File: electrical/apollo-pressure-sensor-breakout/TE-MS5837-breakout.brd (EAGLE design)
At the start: 25 x 36 mm, 12 parts, among them U1 TE-MS5837, X1 RJ45-8-2-CONEC-1, X2 M04X2

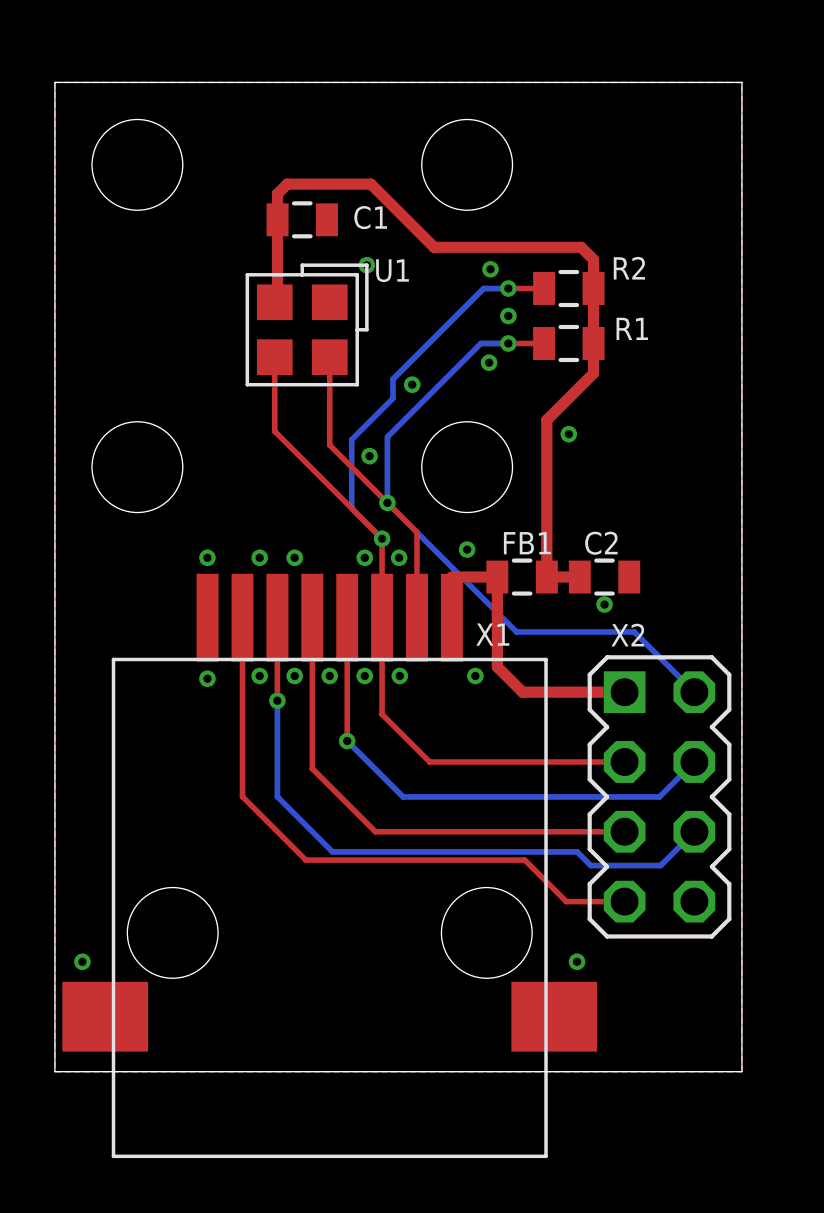
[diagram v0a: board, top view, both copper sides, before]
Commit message: add gerbers to separate directory
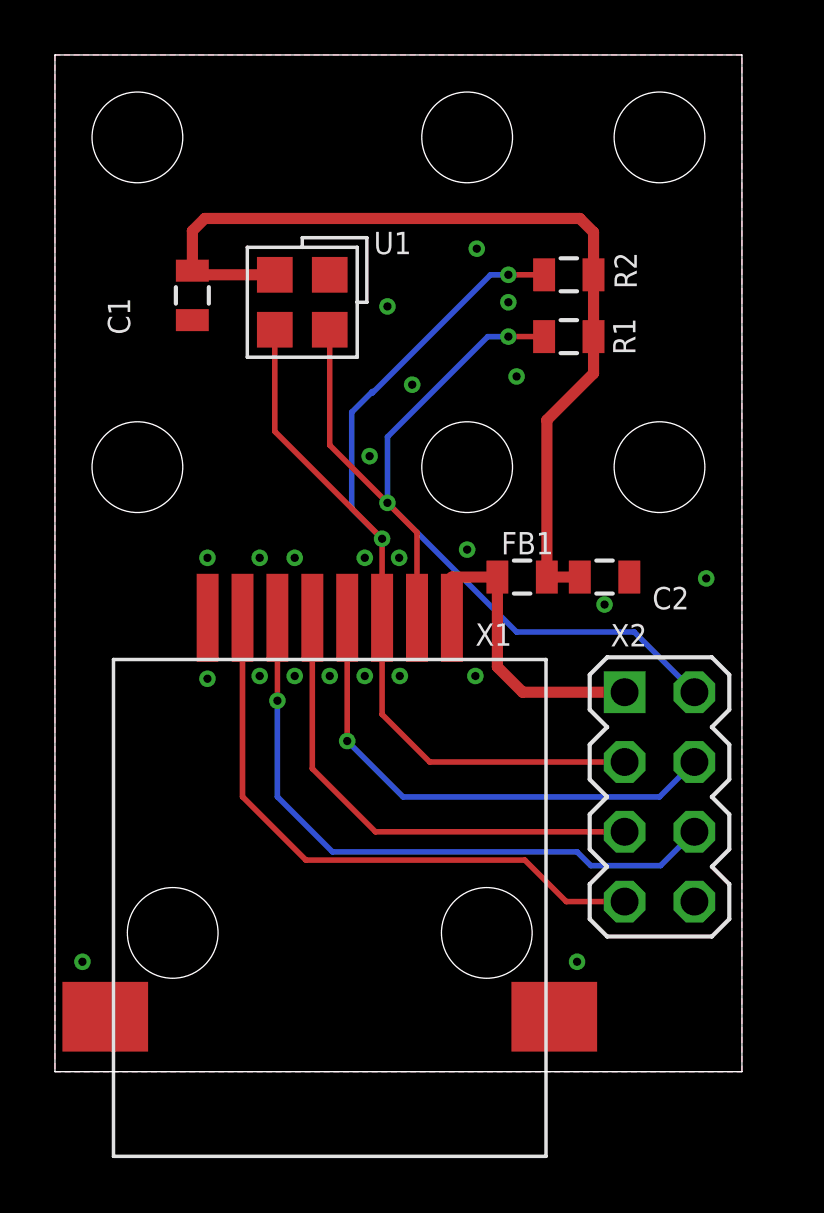
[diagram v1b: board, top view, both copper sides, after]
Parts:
- added JP5, JP6: STAND-OFF, apollo-ctrl:STAND-OFF
- moved C1 4.85 mm to (5.00, 28.2), turned to 270 degrees
- moved JP1 1.00 mm to (3.00, 34.0)
- moved JP2 1.00 mm to (15.0, 34.0)
- moved U1 1.00 mm to (9.00, 28.0)
- moved R2 0.50 mm to (18.7, 29.0)
- moved R1 0.25 mm to (18.7, 26.8)
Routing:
- net 3.3V: track 30.3 -> 34.1 mm
- net SCL: track 37.9 -> 39.4 mm
- net SDA: track 34.3 -> 35.4 mm
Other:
- board size 25 x 36 mm -> 25 x 37 mm
- board text added: "TE MS5837 board Rev. C"

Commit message: resize TE board, add mounting holes
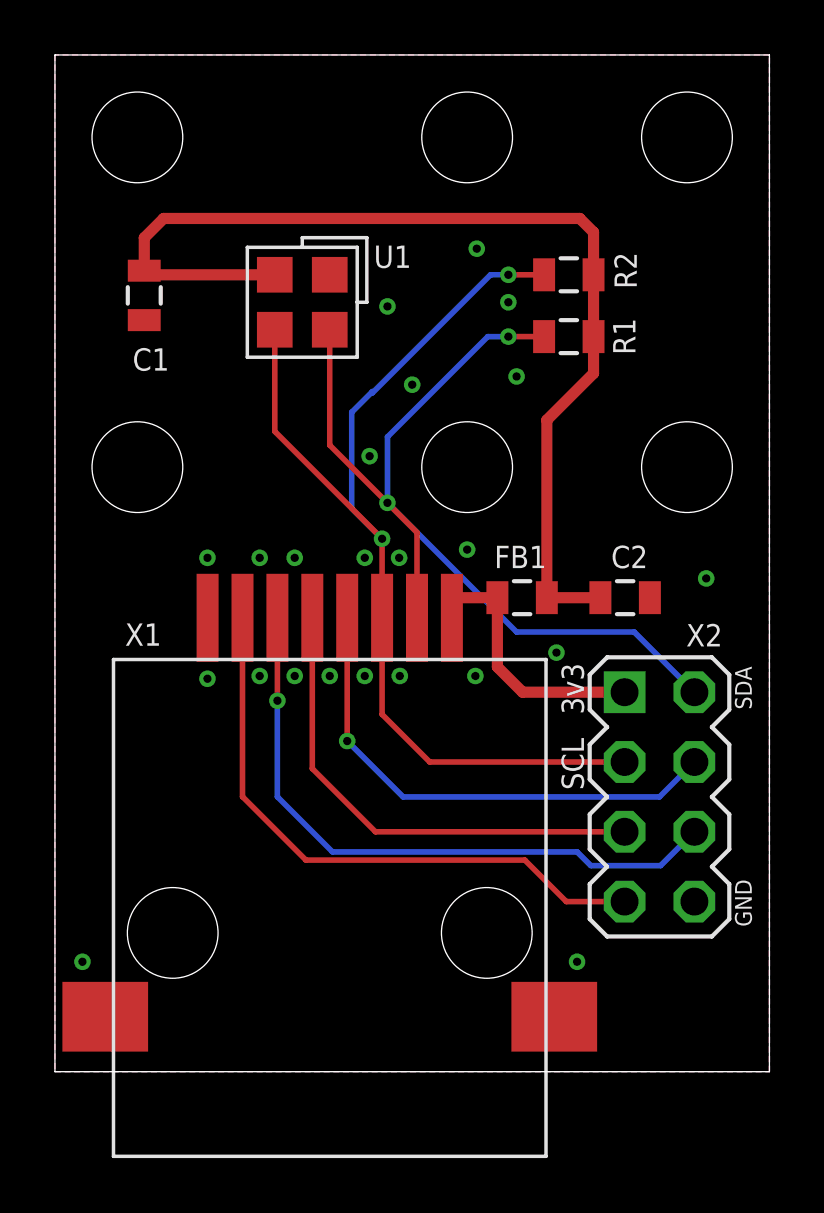
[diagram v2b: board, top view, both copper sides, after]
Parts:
- moved C1 1.75 mm to (3.25, 28.2)
- moved C2 1.06 mm to (20.8, 17.2)
- moved JP5 1.00 mm to (23.0, 34.0)
- moved JP6 1.00 mm to (23.0, 22.0)
- moved FB1 0.75 mm to (17.0, 17.2)
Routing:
- net 3.3V: track 34.1 -> 38.9 mm
- net PWR: track 11.4 -> 9.92 mm
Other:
- board size 25 x 37 mm -> 26 x 37 mm
- board text added: "3v3"
- board text added: "GND"
- board text added: "SCL"
- board text added: "SDA"
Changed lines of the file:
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@@
 <board>
 <plain>
-<wire x1="0" y1="0" x2="25" y2="0" width="0" layer="20"/>
-<wire x1="25" y1="0" x2="25" y2="37" width="0" layer="20"/>
-<wire x1="25" y1="37" x2="0" y2="37" width="0" layer="20"/>
+<wire x1="0" y1="0" x2="26" y2="0" width="0" layer="20"/>
+<wire x1="26" y1="0" x2="26" y2="37" width="0" layer="20"/>
+<wire x1="26" y1="37" x2="0" y2="37" width="0" layer="20"/>
 <wire x1="0" y1="37" x2="0" y2="0" width="0" layer="20"/>
-<dimension x1="0" y1="48" x2="25" y2="48" x3="12.5" y3="50" textsize="1.778" layer="48"/>
 <dimension x1="3" y1="41" x2="15" y2="41" x3="9" y3="46" textsize="1.778" layer="48"/>
 <dimension x1="3" y1="37" x2="9" y2="37" x3="6" y3="40" textsize="1.778" layer="48"/>
@@
 <dimension x1="-3.25" y1="28" x2="-3.25" y2="22" x3="-10.75" y3="25" textsize="1.778" layer="47"/>
 <dimension x1="-8.5" y1="37" x2="-8.5" y2="0" x3="-17.5" y3="18.5" textsize="1.778" layer="47"/>
-<text x="13.75" y="16.5" size="1.778" layer="26" rot="MR270">TE MS5837
+<text x="6.5" y="3.75" size="1.778" layer="26" rot="MR90">TE MS5837
 board
 Rev. C</text>
+<text x="19.25" y="13" size="0.8128" layer="25" rot="R90">3v3</text>
+<text x="19.25" y="10.25" size="0.8128" layer="25" rot="R90">SCL</text>
+<text x="24.75" y="14.75" size="0.6096" layer="25" rot="R270">SDA</text>
+<text x="24.75" y="7" size="0.6096" layer="25" rot="R270">GND</text>
+<dimension x1="0" y1="38.25" x2="26" y2="38.25" x3="13" y3="51.5" textsize="0.6096" layer="47"/>
 </plain>
 <attributes>
@@
 </autorouter>
 <elements>
-<element name="C1" library="apollo-ctrl" package="0805" value="100n" x="5" y="28.25" smashed="yes" rot="R270">
-<attribute name="NAME" x="1.9255" y="28.162" size="0.8128" layer="25" font="vector" rot="R270"/>
-<attribute name="VALUE" x="3.053" y="29.616" size="0.8128" layer="27" font="vector" rot="R270"/>
-</element>
-<element name="C2" library="apollo-ctrl" package="0805" value="1u" x="20" y="18" smashed="yes">
-<attribute name="NAME" x="21.738" y="16.8255" size="0.8128" layer="25" font="vector"/>
-<attribute name="VALUE" x="21.684" y="17.803" size="0.8128" layer="27" font="vector"/>
-</element>
-<element name="FB1" library="apollo-ctrl" package="0805" value="FB-0805" x="17" y="18" smashed="yes">
-<attribute name="NAME" x="16.238" y="18.8255" size="0.8128" layer="25" font="vector"/>
+<element name="C1" library="apollo-ctrl" package="0805" value="100n" x="3.25" y="28.25" smashed="yes" rot="R270">
+<attribute name="NAME" x="4.162" y="26.3245" size="0.8128" layer="25" font="vector" rot="R180"/>
+<attribute name="VALUE" x="2.197" y="26.884" size="0.8128" layer="27" font="vector" rot="R90"/>
+</element>
+<element name="C2" library="apollo-ctrl" package="0805" value="1u" x="20.75" y="17.25" smashed="yes">
+<attribute name="NAME" x="20.238" y="18.3255" size="0.8128" layer="25" font="vector"/>
+<attribute name="VALUE" x="19.934" y="15.553" size="0.8128" layer="27" font="vector"/>
+</element>
+<element name="FB1" library="apollo-ctrl" package="0805" value="FB-0805" x="17" y="17.25" smashed="yes">
+<attribute name="NAME" x="15.988" y="18.3255" size="0.8128" layer="25" font="vector"/>
 </element>
 <element name="R1" library="apollo-ctrl" package="0805" value="4K7" x="18.7" y="26.75" smashed="yes">
@@
 </element>
 <element name="X1" library="apollo-ctrl" package="CONEC-33TS3004ST-88001" value="RJ45-8-2-CONEC-1" x="10" y="2" smashed="yes" rot="R180">
-<attribute name="NAME" x="15.3" y="15.5" size="0.8128" layer="25" font="vector"/>
+<attribute name="NAME" x="2.55" y="15.5" size="0.8128" layer="25" font="vector"/>
 </element>
 <element name="X2" library="apollo-ctrl" package="2X4" value="M04X2" x="22" y="10" smashed="yes" rot="R270">
-<attribute name="NAME" x="20.22" y="15.475" size="0.8128" layer="25" font="vector"/>
+<attribute name="NAME" x="22.97" y="15.475" size="0.8128" layer="25" font="vector"/>
 </element>
 <element name="JP1" library="apollo-ctrl" package="STAND-OFF" value="STAND-OFF" x="3" y="34" smashed="yes"/>
@@
 <element name="JP4" library="apollo-ctrl" package="STAND-OFF" value="STAND-OFF" x="15" y="22" smashed="yes"/>
 <element name="U1" library="apollo-ctrl" package="TE-MS5837" value="TE-MS5837" x="9" y="28" smashed="yes" rot="R90">
-<attribute name="NAME" x="11.6" y="29.75" size="0.8128" layer="25"/>
-</element>
-<element name="JP5" library="apollo-ctrl" package="STAND-OFF" value="STAND-OFF" x="22" y="34" smashed="yes"/>
-<element name="JP6" library="apollo-ctrl" package="STAND-OFF" value="STAND-OFF" x="22" y="22" smashed="yes"/>
+<attribute name="NAME" x="11.6" y="29.25" size="0.8128" layer="25"/>
+</element>
+<element name="JP5" library="apollo-ctrl" package="STAND-OFF" value="STAND-OFF" x="23" y="34" smashed="yes"/>
+<element name="JP6" library="apollo-ctrl" package="STAND-OFF" value="STAND-OFF" x="23" y="22" smashed="yes"/>
 </elements>
 <signals>
@@
 <contactref element="R2" pad="2"/>
 <contactref element="R1" pad="2"/>
-<wire x1="17.9" y1="18" x2="17.9" y2="23.712309375" width="0.4064" layer="1"/>
+<wire x1="17.9" y1="17.25" x2="17.9" y2="23.712309375" width="0.4064" layer="1"/>
 <wire x1="17.9" y1="23.712309375" x2="19.6" y2="25.412309375" width="0.4064" layer="1"/>
 <wire x1="19.6" y1="25.412309375" x2="19.6" y2="26.75" width="0.4064" layer="1"/>
-<wire x1="17.9" y1="18" x2="19.1" y2="18" width="0.4064" layer="1"/>
+<wire x1="19.85" y1="17.25" x2="17.9" y2="17.25" width="0.4064" layer="1"/>
 <wire x1="19.6" y1="26.75" x2="19.6" y2="29" width="0.4064" layer="1"/>
 <contactref element="U1" pad="2"/>
-<wire x1="8.1" y1="29" x2="8" y2="29" width="0.2032" layer="1"/>
-<wire x1="5.453553125" y1="31.05" x2="5" y2="30.596446875" width="0.4064" layer="1"/>
-<wire x1="5" y1="29.15" x2="5" y2="30.596446875" width="0.4064" layer="1"/>
-<wire x1="5.453553125" y1="31.05" x2="19.1" y2="31.05" width="0.4064" layer="1"/>
+<wire x1="3.953553125" y1="31.05" x2="3.25" y2="30.346446875" width="0.4064" layer="1"/>
+<wire x1="3.25" y1="29.15" x2="3.25" y2="30.346446875" width="0.4064" layer="1"/>
+<wire x1="3.953553125" y1="31.05" x2="19.1" y2="31.05" width="0.4064" layer="1"/>
 <wire x1="19.1" y1="31.05" x2="19.6" y2="30.55" width="0.4064" layer="1"/>
 <wire x1="19.6" y1="30.55" x2="19.6" y2="29" width="0.4064" layer="1"/>
-<wire x1="5.03375" y1="29" x2="8" y2="29" width="0.4064" layer="1"/>
-<wire x1="5.03375" y1="29" x2="5" y2="29.15" width="0.4064" layer="1"/>
+<wire x1="3.28375" y1="29" x2="8" y2="29" width="0.4064" layer="1"/>
+<wire x1="3.28375" y1="29" x2="3.25" y2="29.15" width="0.4064" layer="1"/>
 </signal>
 <signal name="GND">
@@
 <polygon width="0.2032" layer="1" spacing="0.2032" isolate="0.2032">
 <vertex x="0" y="0"/>
-<vertex x="25" y="0"/>
-<vertex x="25" y="37"/>
+<vertex x="26" y="0"/>
+<vertex x="26" y="37"/>
 <vertex x="0" y="37"/>
 </polygon>
 <polygon width="0.2032" layer="16" spacing="0.2032" isolate="0.2032">
 <vertex x="0" y="0"/>
-<vertex x="25" y="0"/>
-<vertex x="25" y="37"/>
+<vertex x="26" y="0"/>
+<vertex x="26" y="37"/>
 <vertex x="0" y="37"/>
 </polygon>
@@
 <via x="11.275" y="18.7" extent="1-16" drill="0.3" shape="octagon"/>
 <via x="12.525" y="18.7" extent="1-16" drill="0.3" shape="octagon"/>
-<via x="20" y="17" extent="1-16" drill="0.3" shape="octagon"/>
+<via x="18.25" y="15.25" extent="1-16" drill="0.3" shape="octagon"/>
 <via x="8.725" y="18.7" extent="1-16" drill="0.3" shape="octagon"/>
 <via x="8.725" y="14.4" extent="1-16" drill="0.3" shape="octagon"/>
@@
 <contactref element="FB1" pad="1"/>
 <contactref element="X2" pad="1"/>
-<wire x1="16.1" y1="18" x2="14.445" y2="18" width="0.4064" layer="1"/>
-<wire x1="14.445" y1="18" x2="14.445" y2="16.52" width="0.4064" layer="1"/>
+<wire x1="16.1" y1="17.25" x2="14.445" y2="17.25" width="0.4064" layer="1"/>
+<wire x1="14.445" y1="17.25" x2="14.445" y2="16.52" width="0.4064" layer="1"/>
 <wire x1="20.73" y1="13.81" x2="17.019834375" y2="13.81" width="0.4064" layer="1"/>
 <wire x1="17.019834375" y1="13.81" x2="16.1" y2="14.729834375" width="0.4064" layer="1"/>
-<wire x1="16.1" y1="14.729834375" x2="16.1" y2="18" width="0.4064" layer="1"/>
+<wire x1="16.1" y1="14.729834375" x2="16.1" y2="17.25" width="0.4064" layer="1"/>
 </signal>
 <signal name="SDA">
